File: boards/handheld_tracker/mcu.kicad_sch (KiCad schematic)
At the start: 7 parts, among them U3 ATmega328PB-A, Y1 Crystal

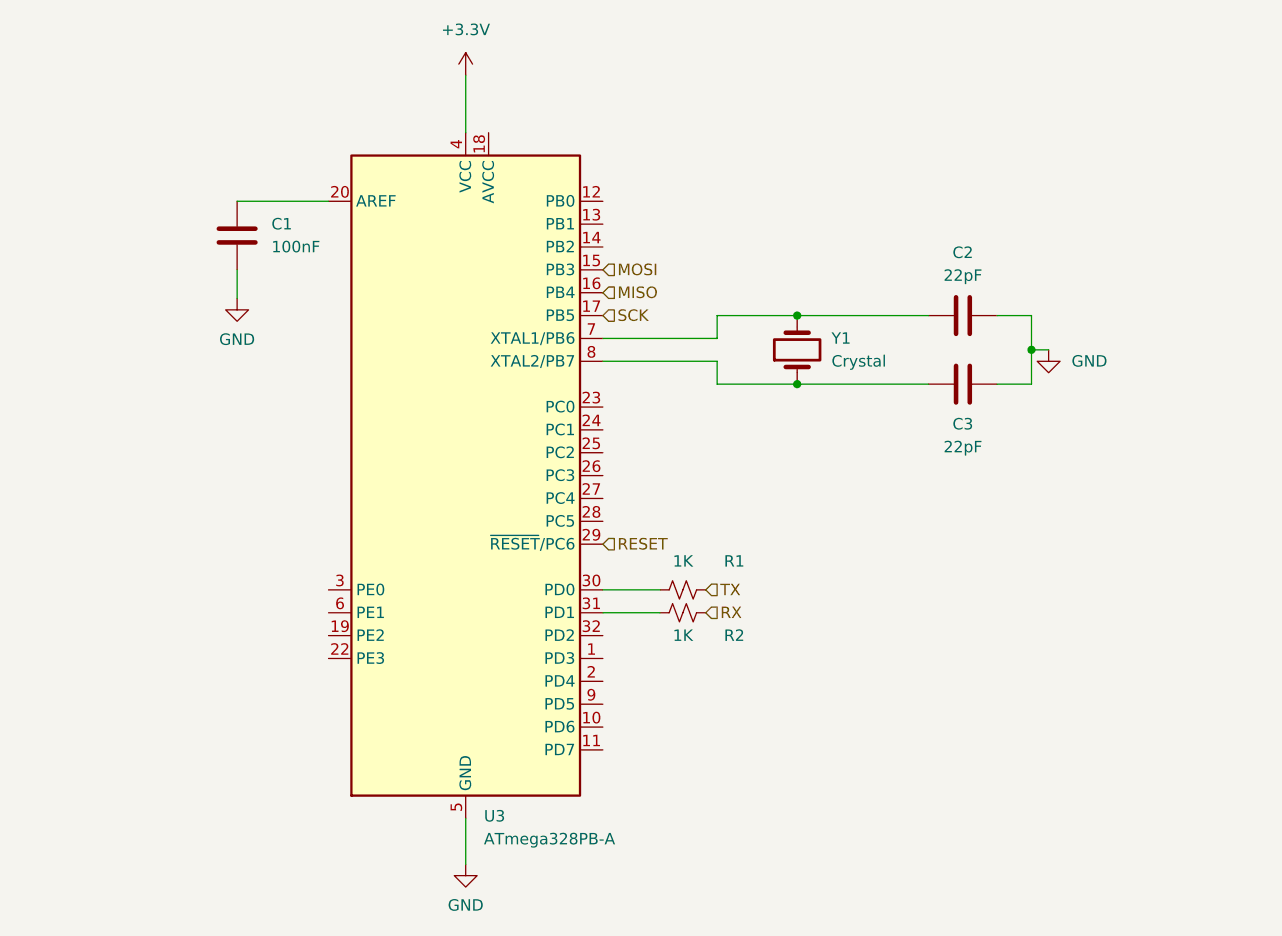
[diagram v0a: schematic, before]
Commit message: added test pads, UI buttons, and routed MCU pins
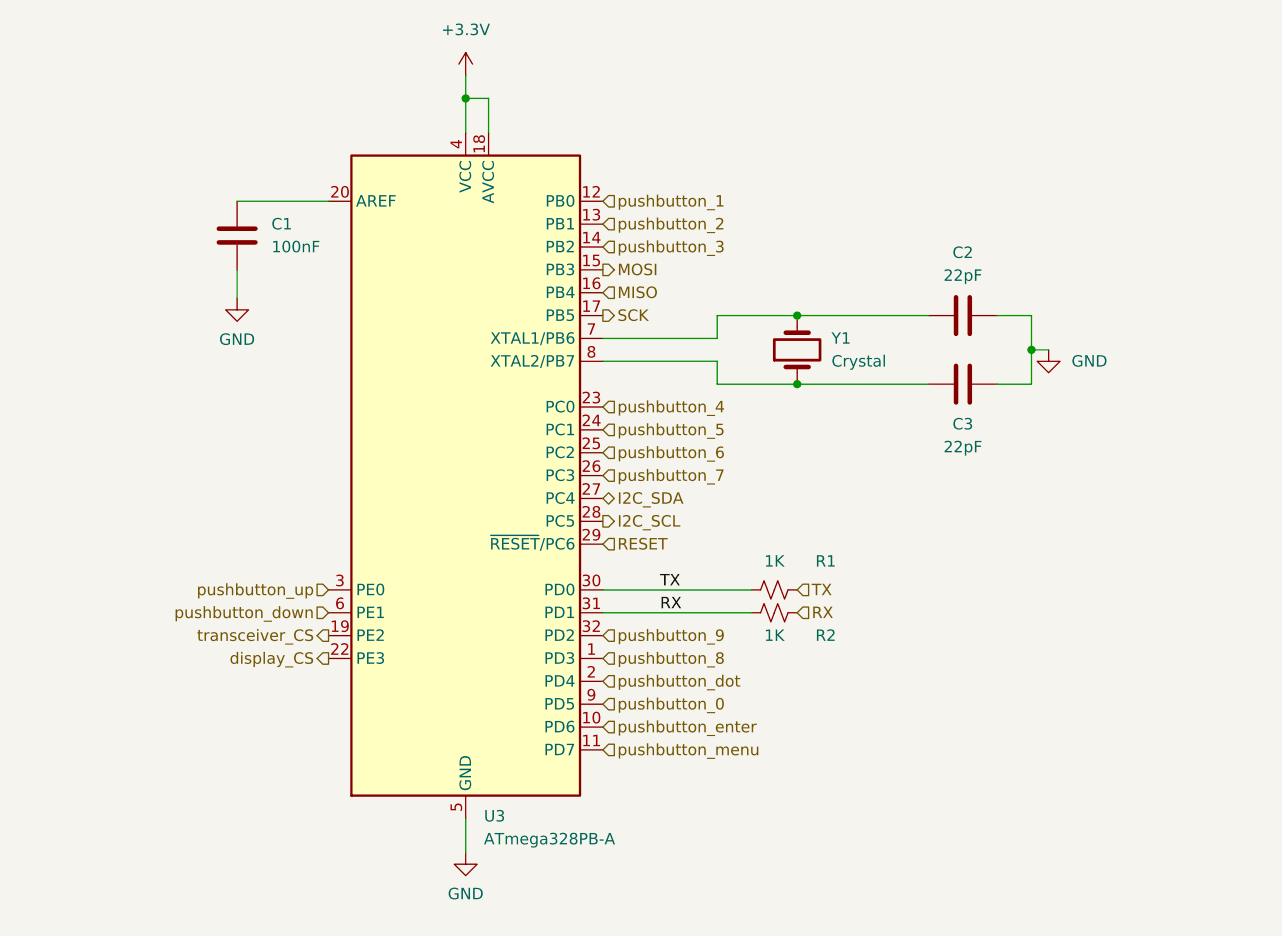
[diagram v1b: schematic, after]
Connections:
- net +3.3V: now also U3.18 (AVCC)
- net RX: now also R2.1, U3.31 (PD1)
- net TX: now also R1.1, U3.30 (PD0)
- net pushbutton_8: now reaches U3.1 (PD3)
- net pushbutton_enter: now reaches U3.10 (PD6)
- net pushbutton_menu: now reaches U3.11 (PD7)
- net pushbutton_1: now reaches U3.12 (PB0)
- net pushbutton_2: now reaches U3.13 (PB1)
- net pushbutton_3: now reaches U3.14 (PB2)
- net transceiver_CS: now reaches U3.19 (PE2)
- net pushbutton_dot: now reaches U3.2 (PD4)
- net display_CS: now reaches U3.22 (PE3)
- net pushbutton_4: now reaches U3.23 (PC0)
- net pushbutton_5: now reaches U3.24 (PC1)
- net pushbutton_6: now reaches U3.25 (PC2)
- net pushbutton_7: now reaches U3.26 (PC3)
- net I2C_SDA: now reaches U3.27 (PC4)
- net I2C_SCL: now reaches U3.28 (PC5)
- net pushbutton_up: now reaches U3.3 (PE0)
- net pushbutton_9: now reaches U3.32 (PD2)
- net pushbutton_down: now reaches U3.6 (PE1)
- net pushbutton_0: now reaches U3.9 (PD5)
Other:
- moved on the sheet: R1, R2

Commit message: added all footprints and modified gitignore
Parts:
- C1, C2, C3: footprint (none) -> Capacitor_SMD:C_0805_2012Metric
- R1, R2: footprint (none) -> Resistor_SMD:R_0805_2012Metric
- Y1: footprint (none) -> footprints:XTAL_ABLS-16_ABR
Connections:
- net display_CS renamed display_RST
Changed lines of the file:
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@@
 		)
 	)
-	(hierarchical_label "display_CS"
+	(hierarchical_label "display_RST"
 		(shape output)
 		(at 116.84 102.87 180)
@@
 			)
 		)
-		(property "Footprint" ""
+		(property "Footprint" "footprints:XTAL_ABLS-16_ABR"
 			(at 168.91 68.58 0)
 			(effects
@@
 			)
 		)
-		(property "Footprint" ""
+		(property "Footprint" "Resistor_SMD:R_0805_2012Metric"
 			(at 166.37 97.79 0)
 			(effects
@@
 			)
 		)
-		(property "Footprint" ""
+		(property "Footprint" "Capacitor_SMD:C_0805_2012Metric"
 			(at 191.135 63.8048 0)
 			(effects
@@
 			)
 		)
-		(property "Footprint" ""
+		(property "Footprint" "Capacitor_SMD:C_0805_2012Metric"
 			(at 191.135 71.4248 0)
 			(effects
@@
 			)
 		)
-		(property "Footprint" ""
+		(property "Footprint" "Resistor_SMD:R_0805_2012Metric"
 			(at 166.37 95.25 0)
 			(effects
@@
 			)
 		)
-		(property "Footprint" ""
+		(property "Footprint" "Capacitor_SMD:C_0805_2012Metric"
 			(at 105.7148 52.07 0)
 			(effects

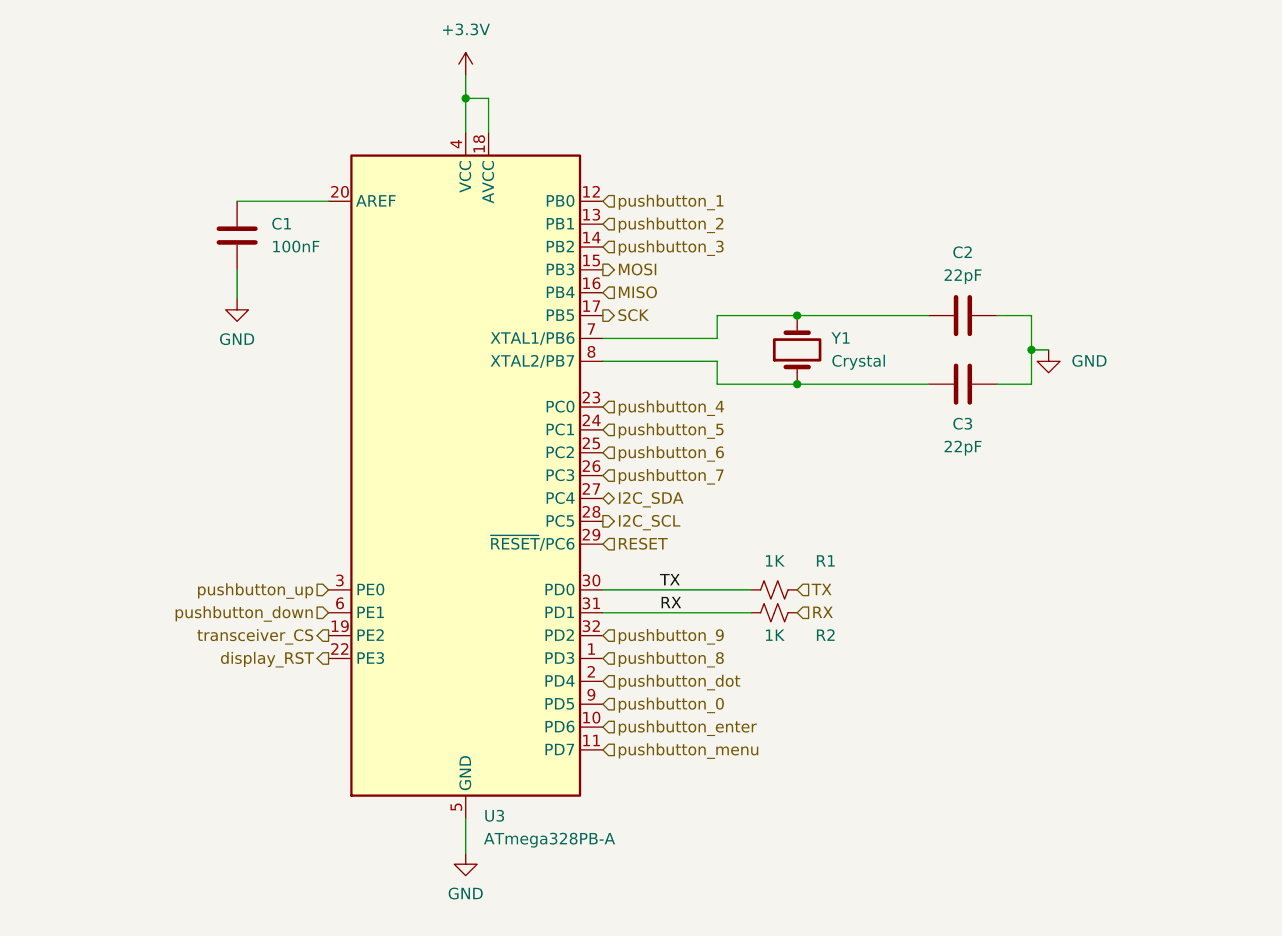
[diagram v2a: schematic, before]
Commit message: added traces for buttons
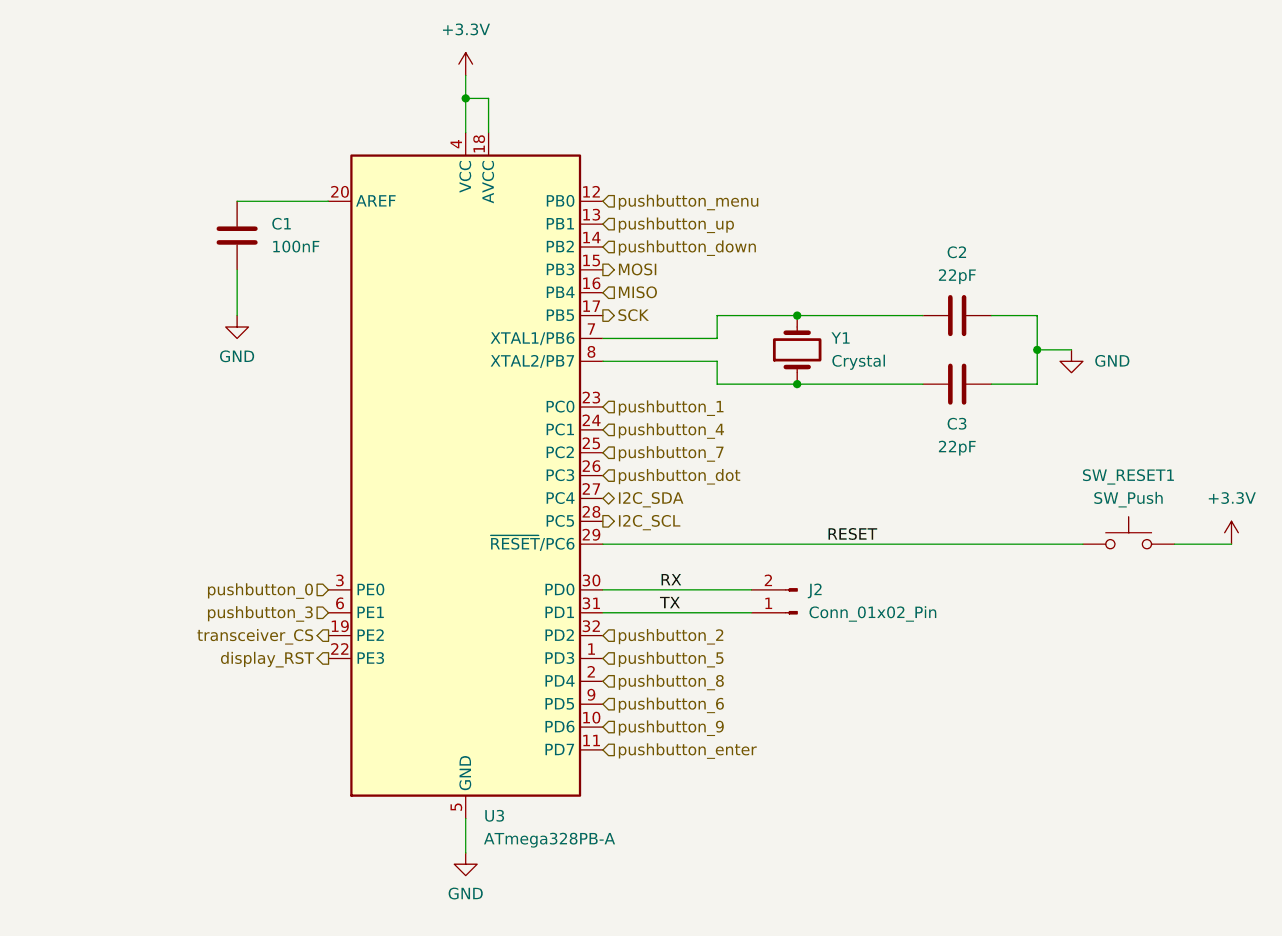
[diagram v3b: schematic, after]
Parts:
- removed R1, R2: 1K, Resistor_SMD:R_0805_2012Metric, symbol Device:R_Small_US
- added J2: Conn_01x02_Pin, symbol Connector:Conn_01x02_Pin
- added SW_RESET1: SW_Push, Button_Switch_SMD:SW_SPST_PTS645, symbol Switch:SW_Push
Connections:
- net +3.3V: now also SW_RESET1.1
- net RESET: now also SW_RESET1.2
- net RX: now also U3.30 (PD0), J2.2 (Pin_2); no longer U3.31 (PD1)
- net TX: now also U3.31 (PD1), J2.1 (Pin_1); no longer U3.30 (PD0)
- net pushbutton_0: now also U3.3 (PE0); no longer U3.9 (PD5)
- net pushbutton_1: now also U3.23 (PC0); no longer U3.12 (PB0)
- net pushbutton_2: now also U3.32 (PD2); no longer U3.13 (PB1)
- net pushbutton_3: now also U3.6 (PE1); no longer U3.14 (PB2)
- net pushbutton_4: now also U3.24 (PC1); no longer U3.23 (PC0)
- net pushbutton_5: now also U3.1 (PD3); no longer U3.24 (PC1)
- net pushbutton_6: now also U3.9 (PD5); no longer U3.25 (PC2)
- net pushbutton_7: now also U3.25 (PC2); no longer U3.26 (PC3)
- net pushbutton_8: now also U3.2 (PD4); no longer U3.1 (PD3)
- net pushbutton_9: now also U3.10 (PD6); no longer U3.32 (PD2)
- net pushbutton_dot: now also U3.26 (PC3); no longer U3.2 (PD4)
- net pushbutton_down: now also U3.14 (PB2); no longer U3.6 (PE1)
- net pushbutton_enter: now also U3.11 (PD7); no longer U3.10 (PD6)
- net pushbutton_menu: now also U3.12 (PB0); no longer U3.11 (PD7)
- net pushbutton_up: now also U3.13 (PB1); no longer U3.3 (PE0)
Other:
- moved on the sheet: C2, C3

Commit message: almost all stuff added and traced, just need proper 3.3 and GND planes plus the mounting holes I think
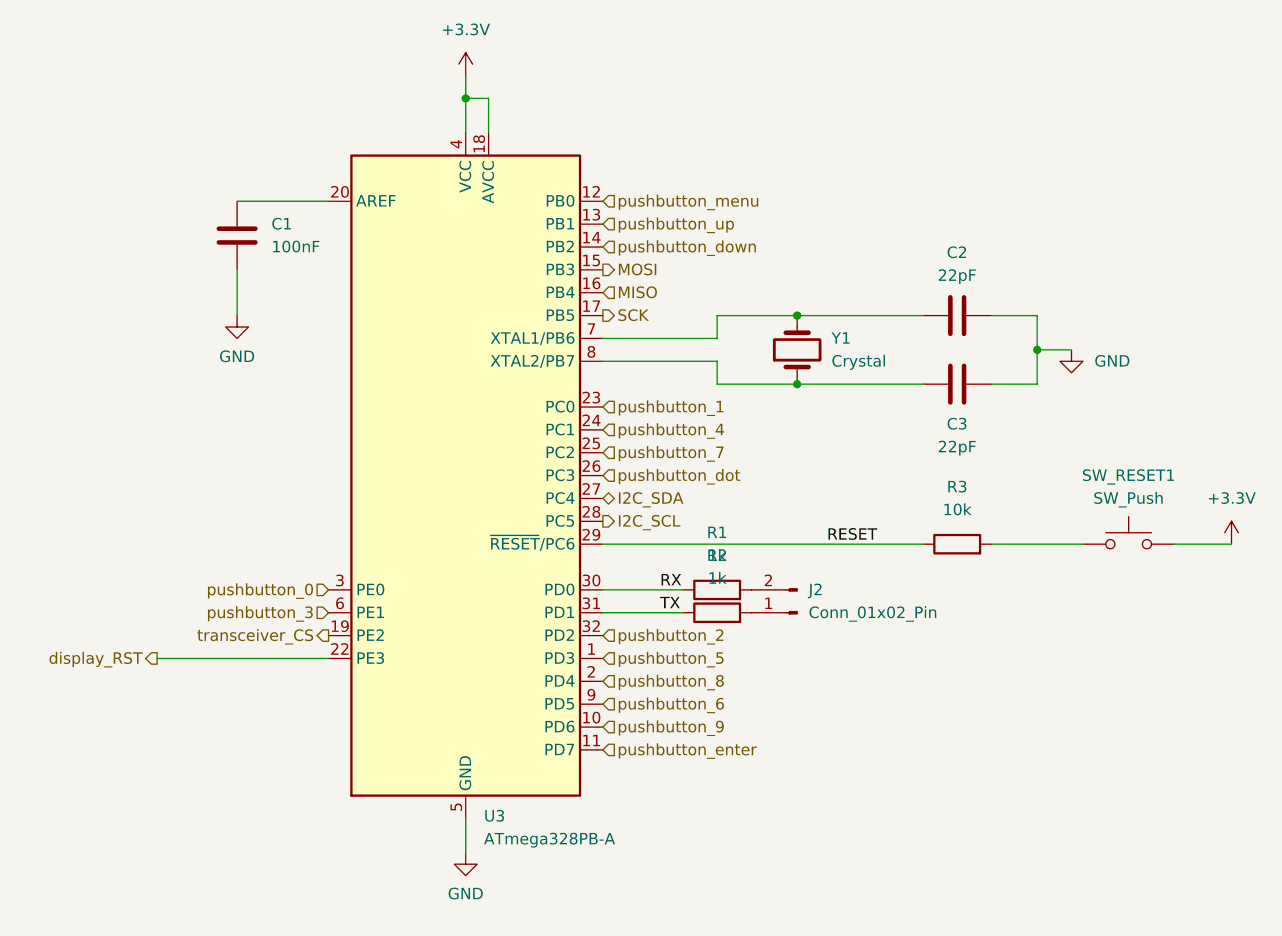
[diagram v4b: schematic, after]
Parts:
- added R1, R2: 1k, Resistor_SMD:R_0805_2012Metric, symbol Device:R
- added R3: 10k, Resistor_SMD:R_0805_2012Metric, symbol Device:R
- J2: footprint (none) -> Connector_PinHeader_2.54mm:PinHeader_1x02_P2.54mm_Vertical
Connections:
- net RESET: now also R3.1; no longer SW_RESET1.2
- net RX: now also R1.1; no longer J2.2 (Pin_2)
- net TX: now also R2.1; no longer J2.1 (Pin_1)
- new net: J2.1 (Pin_1), R2.2
- new net: J2.2 (Pin_2), R1.2
- new net: R3.2, SW_RESET1.2
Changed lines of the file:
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@@
+	(wire
+		(pts
+			(xy 190.5 90.17) (xy 200.66 90.17)
+		)
+		(stroke
+			(width 0)
+			(type default)
+		)
+	)
 	(wire
 		(pts
@@
 	(wire
 		(pts
-			(xy 147.32 90.17) (xy 200.66 90.17)
+			(xy 147.32 90.17) (xy 182.88 90.17)
 		)
 		(stroke
@@
 	(wire
 		(pts
-			(xy 147.32 95.25) (xy 163.83 95.25)
+			(xy 147.32 95.25) (xy 156.21 95.25)
 		)
 		(stroke
@@
 	(wire
 		(pts
-			(xy 147.32 97.79) (xy 163.83 97.79)
+			(xy 147.32 97.79) (xy 156.21 97.79)
 		)
 		(stroke
@@
 		(pts
 			(xy 195.58 72.39) (xy 195.58 68.58)
+		)
+		(stroke
+			(width 0)
+			(type default)
+		)
+	)
+	(wire
+		(pts
+			(xy 97.79 102.87) (xy 116.84 102.87)
 		)
 		(stroke
@@
 	(hierarchical_label "display_RST"
 		(shape output)
-		(at 116.84 102.87 180)
+		(at 97.79 102.87 180)
 		(fields_autoplaced yes)
 		(effects
@@
 			)
 		)
-		(property "Footprint" ""
+		(property "Footprint" "Connector_PinHeader_2.54mm:PinHeader_1x02_P2.54mm_Vertical"
 			(at 168.91 97.79 0)
 			(effects
@@
 				(path "/0d71301b-e65e-49f8-81f9-e7516dc11624/b5768583-2921-450f-a3c7-6bb918f05112"
 					(reference "J2")
+					(unit 1)
+				)
+			)
+		)
+	)
+	(symbol
+		(lib_id "Device:R")
+		(at 186.69 90.17 90)
+		(unit 1)
+		(exclude_from_sim no)
+		(in_bom yes)
+		(on_board yes)
+		(dnp no)
+		(fields_autoplaced yes)
+		(property "Reference" "R3"
+			(at 186.69 83.82 90)
+			(effects
+				(font
+					(size 1.27 1.27)
+				)
+			)
+		)
+		(property "Value" "10k"
+			(at 186.69 86.36 90)
+			(effects
+				(font
+					(size 1.27 1.27)
+				)
+			)
+		)
+		(property "Footprint" "Resistor_SMD:R_0805_2012Metric"
+			(at 186.69 91.948 90)
+			(effects
+				(font
+					(size 1.27 1.27)
+				)
+				(hide yes)
+			)
+		)
+		(property "Datasheet" "~"
+			(at 186.69 90.17 0)
+			(effects
+				(font
+					(size 1.27 1.27)
+				)
+				(hide yes)
+			)
+		)
+		(property "Description" "Resistor"
+			(at 186.69 90.17 0)
+			(effects
+				(font
+					(size 1.27 1.27)
+				)
+				(hide yes)
+			)
+		)
+		(pin "1"
+		)
+		(pin "2"
+		)
+		(instances
+			(project "handheld_tracker"
+				(path "/0d71301b-e65e-49f8-81f9-e7516dc11624/b5768583-2921-450f-a3c7-6bb918f05112"
+					(reference "R3")
 					(unit 1)
 				)
@@
 					(unit 1)
 				)
+			)
+		)
+	)
+	(symbol
+		(lib_id "Device:R")
+		(at 160.02 95.25 90)
+		(unit 1)
+		(exclude_from_sim no)
+		(in_bom yes)
+		(on_board yes)
+		(dnp no)
+		(fields_autoplaced yes)
+		(property "Reference" "R1"
+			(at 160.02 88.9 90)
+			(effects
+				(font
+					(size 1.27 1.27)
+				)
+			)
+		)
+		(property "Value" "1k"
+			(at 160.02 91.44 90)
+			(effects
+				(font
+					(size 1.27 1.27)
+				)
+			)
+		)
+		(property "Footprint" "Resistor_SMD:R_0805_2012Metric"
+			(at 160.02 97.028 90)
+			(effects
+				(font
+					(size 1.27 1.27)
+				)
+				(hide yes)
+			)
+		)
+		(property "Datasheet" "~"
+			(at 160.02 95.25 0)
+			(effects
+				(font
+					(size 1.27 1.27)
+				)
+				(hide yes)
+			)
+		)
+		(property "Description" "Resistor"
+			(at 160.02 95.25 0)
+			(effects
+				(font
+					(size 1.27 1.27)
+				)
+				(hide yes)
+			)
+		)
+		(pin "2"
+		)
+		(pin "1"
+		)
+		(instances
+			(project "handheld_tracker"
+				(path "/0d71301b-e65e-49f8-81f9-e7516dc11624/b5768583-2921-450f-a3c7-6bb918f05112"
+					(reference "R1")
+					(unit 1)
+				)
+			)
+		)
+	)
+	(symbol
+		(lib_id "Device:R")
+		(at 160.02 97.79 90)
+		(unit 1)
+		(exclude_from_sim no)
+		(in_bom yes)
+		(on_board yes)
+		(dnp no)
+		(fields_autoplaced yes)
+		(property "Reference" "R2"
+			(at 160.02 91.44 90)
+			(effects
+				(font
+					(size 1.27 1.27)
+				)
+			)
+		)
+		(property "Value" "1k"
+			(at 160.02 93.98 90)
+			(effects
+				(font
+					(size 1.27 1.27)
+				)
+			)
+		)
+		(property "Footprint" "Resistor_SMD:R_0805_2012Metric"
+			(at 160.02 99.568 90)
+			(effects
+				(font
+					(size 1.27 1.27)
+				)
+				(hide yes)
+			)
+		)
+		(property "Datasheet" "~"
+			(at 160.02 97.79 0)
+			(effects
+				(font
+					(size 1.27 1.27)
+				)
+				(hide yes)
+			)
+		)
+		(property "Description" "Resistor"
+			(at 160.02 97.79 0)
+			(effects
+				(font
+					(size 1.27 1.27)
+				)
+				(hide yes)
+			)
+		)
+		(pin "2"
+		)
+		(pin "1"
+		)
+		(instances
+			(project "handheld_tracker"
+				(path "/0d71301b-e65e-49f8-81f9-e7516dc11624/b5768583-2921-450f-a3c7-6bb918f05112"
+					(reference "R2")
+					(unit 1)
+				)
